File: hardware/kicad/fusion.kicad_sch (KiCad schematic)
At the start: 0 parts

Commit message: Power system schematic
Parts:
- added C1, C2: 4.7uF, symbol Device:C_Small
- added D1: LED, symbol Device:LED
- added J1: Battery, symbol Connector:Conn_01x02_Female
- added L1: 4.7uH, symbol Device:L
- added R1: R_US, symbol Device:R_US
- added U1: MCP1603, SOT95P280X110-5N, symbol MCP1603:MCP1603
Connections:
- new net: D1.2 (A), R1.1
- new net: L1.1, U1.5 (LX)
- new net +3V3: C2.1, L1.2, R1.2, U1.4 (VFB/VOUT)
- new net GNDREF: C1.2, C2.2, D1.1 (K), J1.1 (Pin_1), U1.2 (GND)
- new net VBAT: C1.1, J1.2 (Pin_2), U1.1 (VIN), U1.3 (~{SHDN})
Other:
- note added: "POWER"

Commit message: IMU SPI header
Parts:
- added J?: Conn_01x06_Male, symbol Connector:Conn_01x06_Male
- added U?: PIC16F690-IP, symbol MCU_Microchip_PIC16:PIC16F690-IP
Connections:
- net +3V3: now also J?.6 (Pin_6), U?.1 (VDD)
- net GNDREF: now also J?.5 (Pin_5), U?.20 (VSS)
- new net CS: J?.1 (Pin_1), U?.8 (RC6/AN8/~{SS})
- new net MISO: J?.2 (Pin_2), U?.13 (SDI/SDA/AN10/RB4)
- new net MOSI: J?.3 (Pin_3), U?.9 (RC7/AN9/SDO)
- new net SCK: J?.4 (Pin_4), U?.11 (SCK/SCL/RB6)
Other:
- note added: "IMU (SPI)"
- moved on the sheet: C1, C2, D1, J1, L1, R1, U1

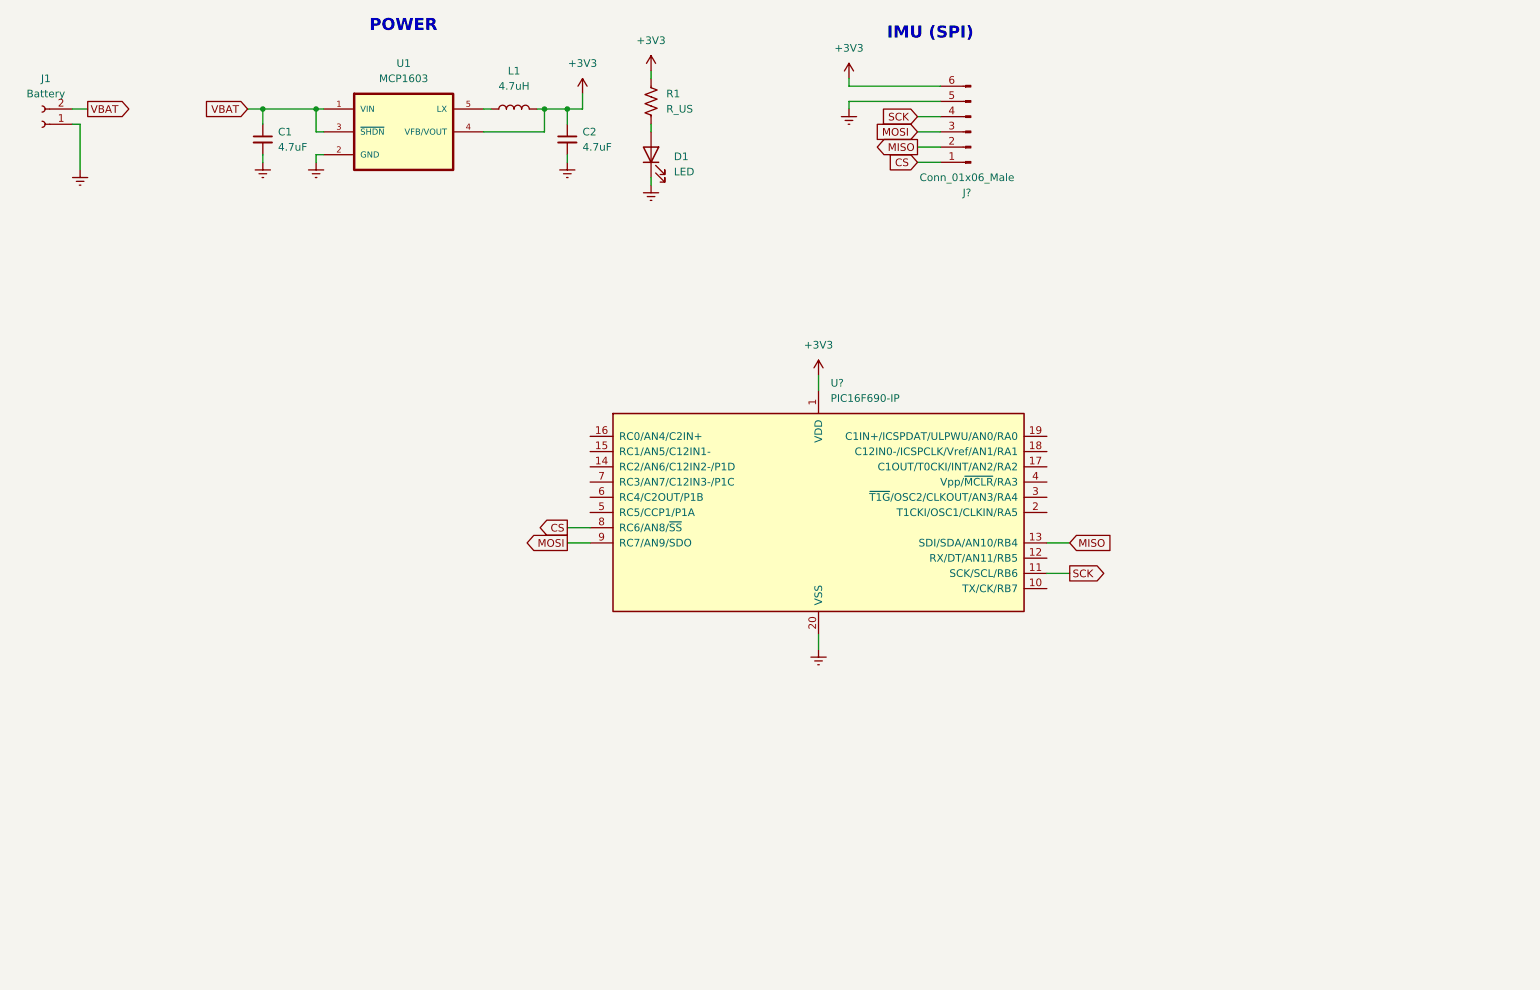
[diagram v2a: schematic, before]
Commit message: Rest of schematic
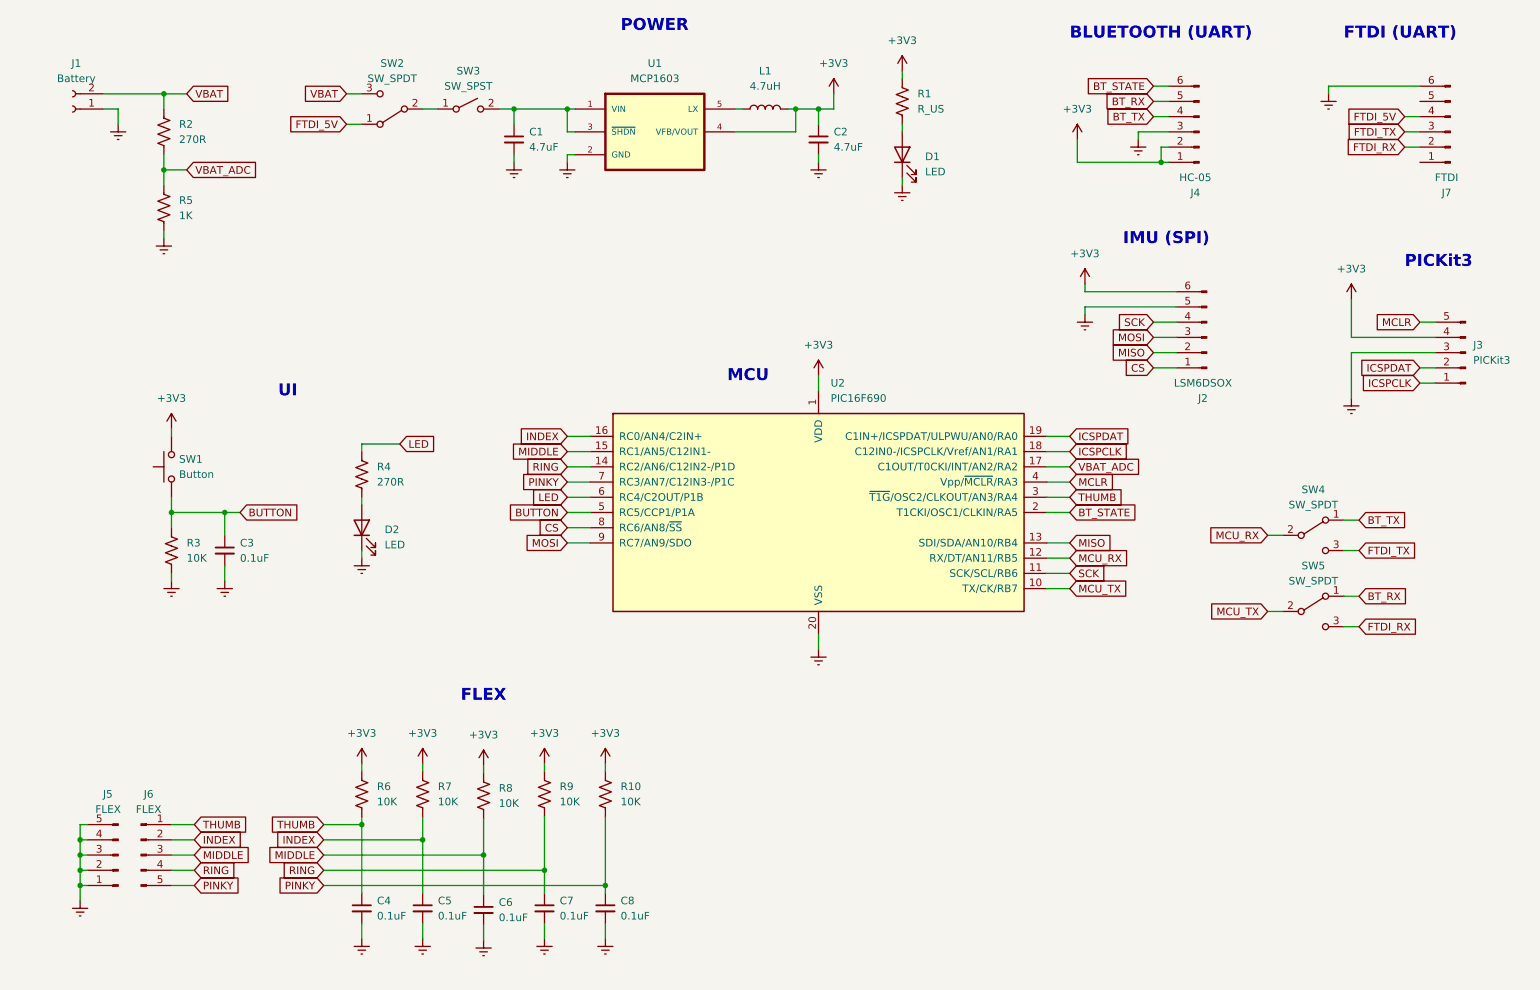
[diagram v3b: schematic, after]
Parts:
- added C3, C4, C5, C6, C7, C8: 0.1uF, symbol Device:C_Small
- added D2: LED, symbol Device:LED
- added J3: PICKit3, symbol Connector:Conn_01x05_Male
- added J4: HC-05, symbol Connector:Conn_01x06_Male
- added J5, J6: FLEX, symbol Connector:Conn_01x05_Male
- added J7: FTDI, symbol Connector:Conn_01x06_Male
- added R10, R3, R6, R7, R8, R9: 10K, symbol Device:R_US
- added R2, R4: 270R, symbol Device:R_US
- added R5: 1K, symbol Device:R_US
- added SW1: Button, symbol Switch:SW_Push
- added SW2, SW4, SW5: SW_SPDT, symbol Switch:SW_SPDT
- added SW3: SW_SPST, symbol Switch:SW_SPST
- J2: renamed from J?; value Conn_01x06_Male -> LSM6DSOX
- U2: renamed from U?; value PIC16F690-IP -> PIC16F690
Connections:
- net +3V3: now also J3.4 (Pin_4), J4.1 (Pin_1), J4.2 (Pin_2), R10.1, R6.1, R7.1, R8.1, R9.1, SW1.2
- net GNDREF: now also C3.2, C4.2, C5.2, C6.2, C7.2, C8.2, D2.1 (K), J3.3 (Pin_3), J4.3 (Pin_3), J5.1 (Pin_1), J5.2 (Pin_2), J5.3 (Pin_3), J5.4 (Pin_4), J5.5 (Pin_5), J7.6 (Pin_6), R3.2, R5.2
- net VBAT: now also R2.1, SW2.3 (C); no longer C1.1, U1.1 (VIN), U1.3 (~{SHDN})
- net MCU_TX: now reaches U2.10 (TX/CK/RB7)
- net MCU_TX: now also SW5.2 (B)
- net MCU_RX: now reaches U2.12 (RX/DT/AN11/RB5)
- net MCU_RX: now also SW4.2 (B)
- net RING: now reaches U2.14 (RC2/AN6/C12IN2-/P1D)
- net RING: now also C7.1, J6.4 (Pin_4), R9.2
- net MIDDLE: now reaches U2.15 (RC1/AN5/C12IN1-)
- net MIDDLE: now also C6.1, J6.3 (Pin_3), R8.2
- net INDEX: now reaches U2.16 (RC0/AN4/C2IN+)
- net INDEX: now also C5.1, J6.2 (Pin_2), R7.2
- net VBAT_ADC: now reaches U2.17 (C1OUT/T0CKI/INT/AN2/RA2)
- net VBAT_ADC: now also R2.2, R5.1
- net ICSPCLK: now reaches U2.18 (C12IN0-/ICSPCLK/Vref/AN1/RA1)
- net ICSPCLK: now also J3.1 (Pin_1)
- net ICSPDAT: now reaches U2.19 (C1IN+/ICSPDAT/ULPWU/AN0/RA0)
- net ICSPDAT: now also J3.2 (Pin_2)
- net BT_STATE: now reaches U2.2 (T1CKI/OSC1/CLKIN/RA5)
- net BT_STATE: now also J4.6 (Pin_6)
- net THUMB: now reaches U2.3 (~{T1G}/OSC2/CLKOUT/AN3/RA4)
- net THUMB: now also C4.1, J6.1 (Pin_1), R6.2
- net MCLR: now reaches U2.4 (Vpp/~{MCLR}/RA3)
- net MCLR: now also J3.5 (Pin_5)
- net BUTTON: now reaches U2.5 (RC5/CCP1/P1A)
- net BUTTON: now also C3.1, R3.1, SW1.1
- net LED: now reaches U2.6 (RC4/C2OUT/P1B)
- net LED: now also R4.2
- net PINKY: now reaches U2.7 (RC3/AN7/C12IN3-/P1C)
- net PINKY: now also C8.1, J6.5 (Pin_5), R10.2
- new net: C1.1, SW3.2 (B), U1.1 (VIN), U1.3 (~{SHDN})
- new net: SW2.2 (B), SW3.1 (A)
- new net: D2.2 (A), R4.1
- new net BT_RX: J4.5 (Pin_5), SW5.1 (A)
- new net BT_TX: J4.4 (Pin_4), SW4.1 (A)
- new net FTDI_5V: J7.4 (Pin_4), SW2.1 (A)
- new net FTDI_RX: J7.2 (Pin_2), SW5.3 (C)
- new net FTDI_TX: J7.3 (Pin_3), SW4.3 (C)
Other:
- note added: "BLUETOOTH (UART)"
- note added: "FLEX"
- note added: "FTDI (UART)"
- note added: "MCU"
- note added: "PICKit3"
- note added: "UI"
- moved on the sheet: C1, C2, D1, J1, J2, L1, R1, U1

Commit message: Connect PIC pin to EN/KEY for BT instead of STATE
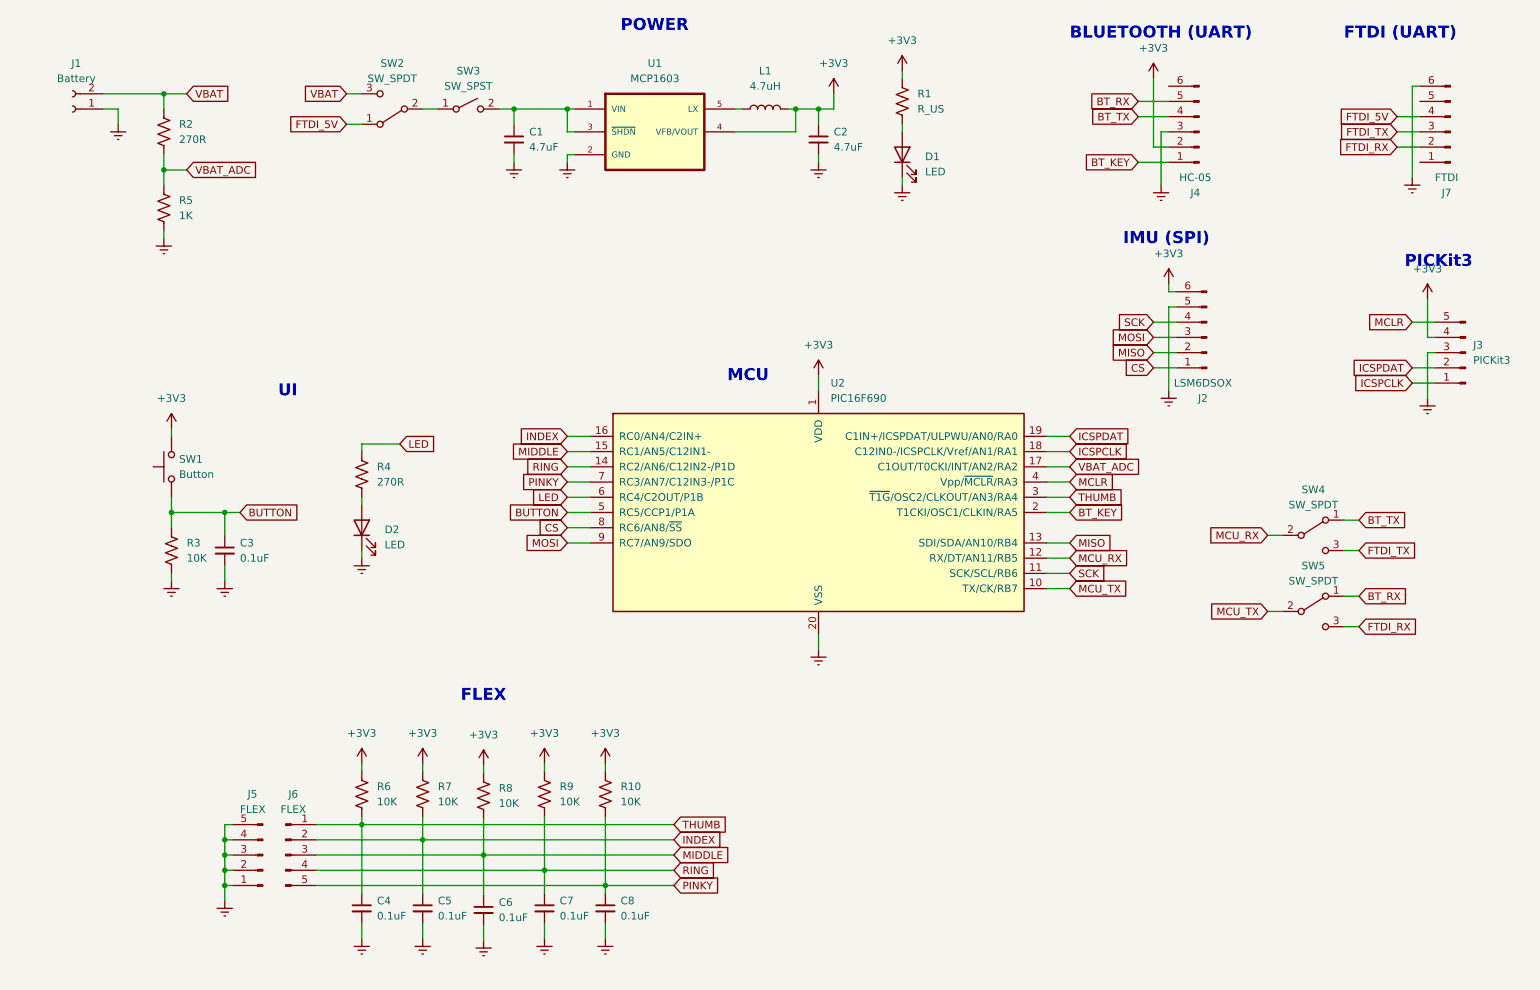
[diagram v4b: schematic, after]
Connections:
- net +3V3: no longer J4.1 (Pin_1)
- net BT_STATE: no longer names the net of J4.6 (Pin_6)
- net BT_STATE: no longer U2.2 (T1CKI/OSC1/CLKIN/RA5)
- new net BT_KEY: J4.1 (Pin_1), U2.2 (T1CKI/OSC1/CLKIN/RA5)
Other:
- moved on the sheet: J5, J6

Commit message: Change battery monitor resistors to handle 5 V with less leakage
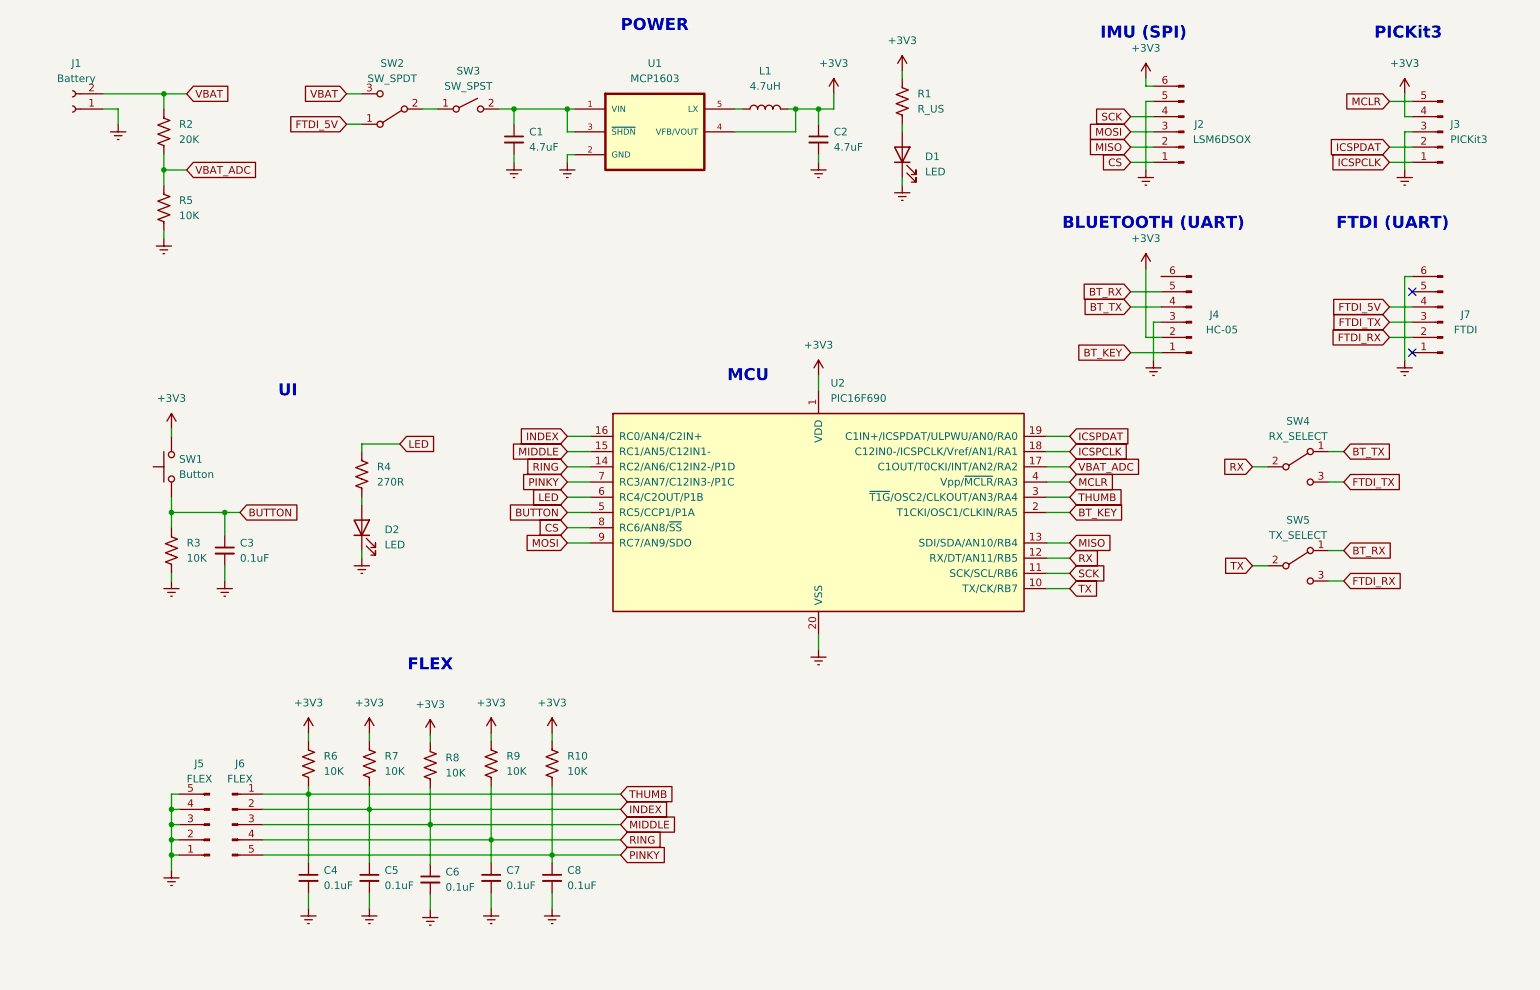
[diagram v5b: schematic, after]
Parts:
- R2: value 270R -> 20K
- R5: value 1K -> 10K
- SW4: value SW_SPDT -> RX_SELECT
- SW5: value SW_SPDT -> TX_SELECT
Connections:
- net MCU_RX renamed RX
- net MCU_TX renamed TX
- no-connect marks 0 -> 2
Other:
- moved on the sheet: C4, C5, C6, C7, C8, J2, J3, J4, J5, J6, J7, R10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

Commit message: Labels for switches
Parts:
- J3: value PICKit3 -> PICKIT
- R1: value R_US -> 270R
- SW1: value Button -> BUTTON
- SW2: value SW_SPDT -> POWER_SELECT
- SW3: value SW_SPST -> POWER
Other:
- moved on the sheet: J1, R2, R5, SW2, SW3

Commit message: chung's changes
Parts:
- removed SW2: POWER_SELECT, symbol Switch:SW_SPDT
- removed SW3: POWER, symbol Switch:SW_SPST
- removed SW4: RX_SELECT, symbol Switch:SW_SPDT
- removed SW5: TX_SELECT, symbol Switch:SW_SPDT
- added SW2: SW_SP3T, symbol Switch:SW_SP3T
- added SW3: SW_DPDT_x2, symbol Switch:SW_DPDT_x2
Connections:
- net BT_RX: now also SW3.4 (A)
- net BT_TX: now also SW3.1 (A)
- net FTDI_5V: now also SW2.2
- net FTDI_RX: now also SW3.6 (C)
- net FTDI_TX: now also SW3.3 (C)
- net GNDREF: now also R2.2; no longer R5.2
- net RX: now also SW3.2 (B)
- net TX: now also SW3.5 (B)
- net VBAT_ADC: now also R2.1, R5.2; no longer R2.2, R5.1
- net at C1.1, U1.1 (VIN), U1.3 (~{SHDN}): now also R5.1, SW2.3
- net VBAT: no longer names the net of J1.2 (Pin_2)
- net VBAT: now also SW2.4; no longer R2.1
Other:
- moved on the sheet: C3, C4, C5, C6, C7, C8, D2, J1, J5, J6, R10, R3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

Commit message: Select some footprints
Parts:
- removed J4: HC-05, symbol Connector:Conn_01x06_Male
- removed J5, J6: FLEX, symbol Connector:Conn_01x05_Male
- added J4: HC-05, Connector_PinHeader_2.54mm:PinHeader_1x05_P2.54mm_Horizontal, symbol Connector:Conn_01x05_Male
- added J5: FLEX, Connector_PinHeader_2.54mm:PinHeader_2x05_P2.54mm_Horizontal, symbol Connector_Generic:Conn_02x05_Counter_Clockwise
- J1: value Battery -> BATTERY; footprint (none) -> Fusion:JST
- J2, J7: footprint (none) -> Connector_PinHeader_2.54mm:PinHeader_1x06_P2.54mm_Horizontal
- J3: footprint (none) -> Connector_PinHeader_2.54mm:PinHeader_1x05_P2.54mm_Horizontal
- SW1: footprint (none) -> Button_Switch_THT:SW_PUSH_6mm_H5mm
- SW2: value SW_SP3T -> POWER
- SW3: value SW_DPDT_x2 -> UART; footprint (none) -> Button_Switch_THT:SW_CuK_JS202011CQN_DPDT_Straight
- U1: footprint SOT95P280X110-5N -> Package_TO_SOT_SMD:TSOT-23-5_HandSoldering
- U2: footprint (none) -> Package_DIP:DIP-20_W7.62mm_Socket
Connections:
- net +3V3: now also J4.2 (Pin_2)
- net BT_KEY: now also J4.1 (Pin_1)
- net BT_RX: now also J4.5 (Pin_5)
- net BT_TX: now also J4.4 (Pin_4)
- net GNDREF: now also J4.3 (Pin_3), J5.1 (Pin_1), J5.2 (Pin_2), J5.3 (Pin_3), J5.4 (Pin_4), J5.5 (Pin_5)
- net INDEX: now also J5.9 (Pin_9)
- net MIDDLE: now also J5.8 (Pin_8)
- net PINKY: now also J5.6 (Pin_6)
- net RING: now also J5.7 (Pin_7)
- net THUMB: now also J5.10 (Pin_10)
